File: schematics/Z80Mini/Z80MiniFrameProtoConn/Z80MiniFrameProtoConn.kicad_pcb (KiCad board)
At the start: 2 copper layers, 35.6 x 68.6 mm, 4 parts, among them J1 Z80MiniFrame BUS, J2 ROW1, J3 ROW2, J4 DATA

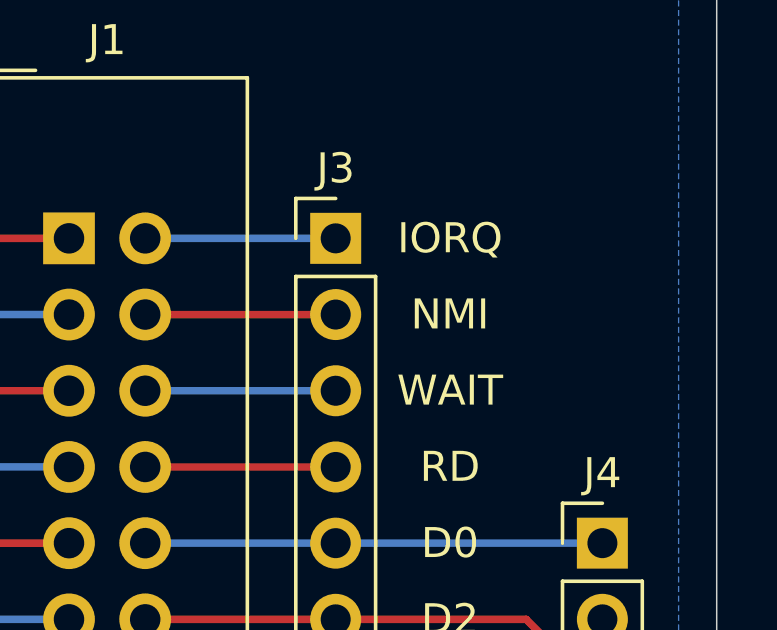
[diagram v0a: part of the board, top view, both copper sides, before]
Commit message: Latest code changes and modified Makefile to support burn to EPROM Emulator
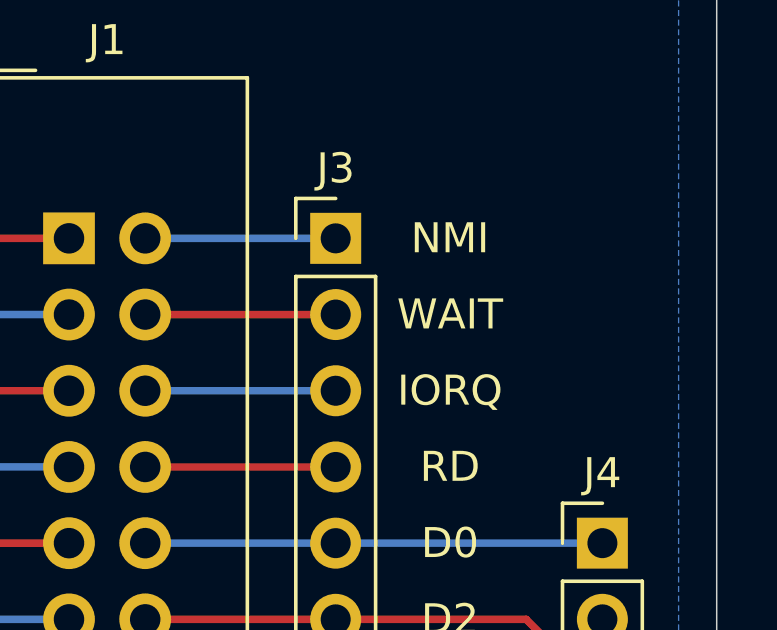
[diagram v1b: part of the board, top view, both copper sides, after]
